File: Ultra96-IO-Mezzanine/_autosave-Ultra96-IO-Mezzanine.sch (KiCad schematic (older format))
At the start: 45 parts, among them J1 USB_C_Receptacle_USB2.0, J2 Conn_01x08_Female, J3 USB_C_Receptacle_USB2.0, P1 CONN_02X20, P2 CONN_02X30, P3 CONN_02X20, Q1 STL6P3LLH6, SW1 SW_SP3T, U1 TXS0104ERGYR, U2 CP2102N-A01-GQFN24, U3 TXS0108EPW, U4 STUSB4500QTR, U5 TXS0108EPW

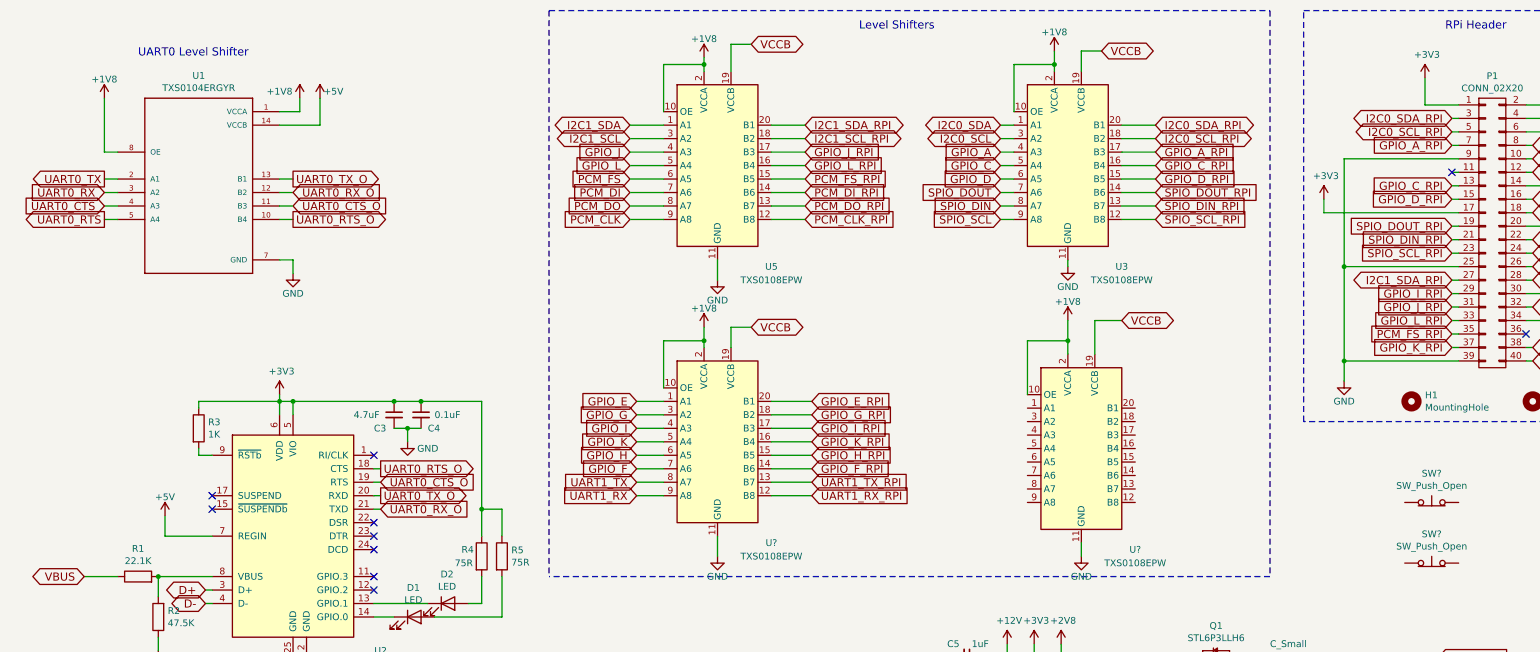
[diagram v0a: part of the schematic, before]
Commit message: Added TXS0108
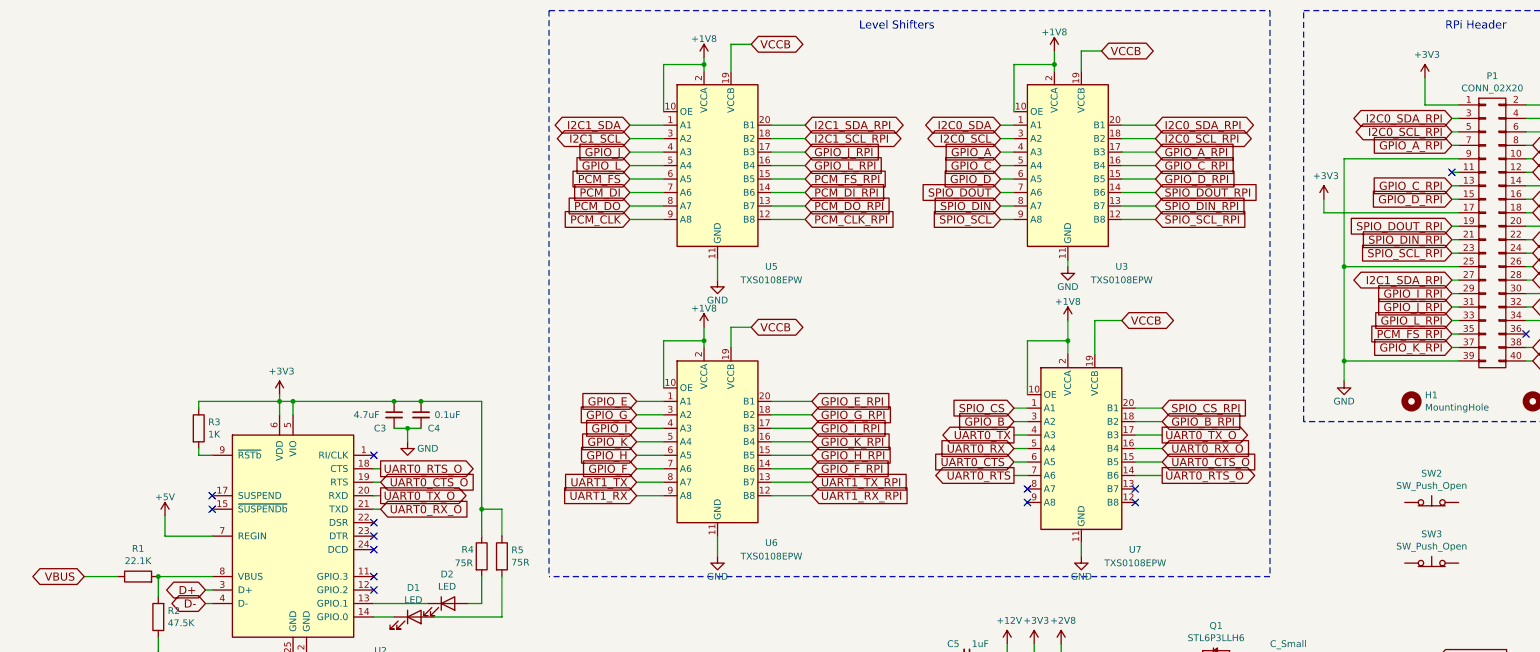
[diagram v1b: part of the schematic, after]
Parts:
- removed U1: TXS0104ERGYR, Package_DFN_QFN:Texas_S-PVQFN-N14_ThermalVias, symbol Ultra96-IO-Mezzanine-rescue:TXS0104ERGYR-LevelShifer
- gave numbers to parts that had none: 4
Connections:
- net GPIO_B: now also U7.3 (A2)
- net GPIO_B_RPI: now also U7.18 (B2)
- net SPIO_CS: now also U7.1 (A1)
- net SPIO_CS_RPI: now also U7.20 (B1)
- net UART0_CTS: now also U7.6 (A5)
- net UART0_CTS_O: now also U7.15 (B5)
- net UART0_RTS: now also U7.7 (A6)
- net UART0_RTS_O: now also U7.14 (B6)
- net UART0_RX: now also U7.5 (A4)
- net UART0_RX_O: now also U7.16 (B4)
- net UART0_TX: now also U7.4 (A3)
- net UART0_TX_O: now also U7.17 (B3)
- no-connect marks 26 -> 30
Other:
- note removed: "UART0 Level Shifter"
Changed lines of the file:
@@
 Wire Notes Line
 	13150 600  13150 4250
-$Comp
-L Ultra96-IO-Mezzanine-rescue:GND-power #PWR07
-U 1 1 5F13E6D4
-P 2900 2550
-F 0 "#PWR07" H 2900 2300 50  0001 C CNN
-F 1 "GND" H 2900 2400 50  0000 C CNN
-F 2 "" H 2900 2550 60  0000 C CNN
-F 3 "" H 2900 2550 60  0000 C CNN
-	1    2900 2550
-	1    0    0    -1
-$EndComp
-Wire Wire Line
-	2900 2450 2900 2550
-Text GLabel 1500 1850 0    60   Output ~ 0
+Text GLabel 8250 3750 0    60   Output ~ 0
 UART0_TX
 Wire Wire Line
-	1500 1850 1600 1850
-Text GLabel 1500 1950 0    60   Input ~ 0
+	8250 3750 8350 3750
+Text GLabel 8250 3850 0    60   Input ~ 0
 UART0_RX
 Wire Wire Line
-	1500 1950 1600 1950
-Text GLabel 1500 2050 0    60   Input ~ 0
+	8250 3850 8350 3850
+Text GLabel 8250 3950 0    60   Input ~ 0
 UART0_CTS
 Wire Wire Line
-	1500 2050 1600 2050
-Text GLabel 1500 2150 0    60   Output ~ 0
+	8250 3950 8350 3950
+Text GLabel 8250 4050 0    60   Output ~ 0
 UART0_RTS
 Wire Wire Line
-	1500 2150 1600 2150
-$Comp
-L Ultra96-IO-Mezzanine-rescue:+5V-power #PWR010
-U 1 1 5F1655F2
-P 3100 1250
-F 0 "#PWR010" H 3100 1100 50  0001 C CNN
-F 1 "+5V" H 3200 1300 50  0000 C CNN
-F 2 "" H 3100 1250 50  0001 C CNN
-F 3 "" H 3100 1250 50  0001 C CNN
-	1    3100 1250
-	1    0    0    -1
-$EndComp
-Text GLabel 2900 1850 2    60   Output ~ 0
+	8250 4050 8350 4050
+Text GLabel 9350 3750 2    60   Output ~ 0
 UART0_TX_O
-Wire Wire Line
-	2900 1850 2800 1850
-Text GLabel 2900 1950 2    60   Input ~ 0
+Text GLabel 9350 3850 2    60   Input ~ 0
 UART0_RX_O
-Wire Wire Line
-	2900 1950 2800 1950
-Text GLabel 2900 2050 2    60   Input ~ 0
+Text GLabel 9350 3950 2    60   Input ~ 0
 UART0_CTS_O
-Wire Wire Line
-	2900 2050 2800 2050
-Text GLabel 2900 2150 2    60   Output ~ 0
+Text GLabel 9350 4050 2    60   Output ~ 0
 UART0_RTS_O
-Wire Wire Line
-	2900 2150 2800 2150
-$Comp
-L Ultra96-IO-Mezzanine-rescue:TXS0104ERGYR-LevelShifer U1
-U 1 1 5F19EA6D
-P 2200 1950
-F 0 "U1" H 2200 2817 50  0000 C CNN
-F 1 "TXS0104ERGYR" H 2200 2726 50  0000 C CNN
-F 2 "Package_DFN_QFN:Texas_S-PVQFN-N14_ThermalVias" H 2200 1950 50  0001 L BNN
-F 3 "TEXAS INSTRUMENTS" H 2200 1950 50  0001 L BNN
-F 4 "IPC 7351B" H 2200 1950 50  0001 L BNN "Field4"
-F 5 "H" H 2200 1950 50  0001 L BNN "Field5"
-	1    2200 1950
-	1    0    0    -1
-$EndComp
-Wire Wire Line
-	2950 1250 2950 1350
-$Comp
-L Ultra96-IO-Mezzanine-rescue:+1V8-power #PWR09
-U 1 1 5F143AFB
-P 2950 1250
-F 0 "#PWR09" H 2950 1100 50  0001 C CNN
-F 1 "+1V8" H 2800 1300 50  0000 C CNN
-F 2 "" H 2950 1250 60  0000 C CNN
-F 3 "" H 2950 1250 60  0000 C CNN
-	1    2950 1250
-	1    0    0    -1
-$EndComp
-Wire Wire Line
-	2800 1350 2950 1350
-Wire Wire Line
-	2800 1450 3100 1450
-Wire Wire Line
-	3100 1250 3100 1450
-Wire Wire Line
-	2900 2450 2800 2450
-$Comp
-L Ultra96-IO-Mezzanine-rescue:+1V8-power #PWR03
-U 1 1 5F1F21A8
-P 1500 1250
-F 0 "#PWR03" H 1500 1100 50  0001 C CNN
-F 1 "+1V8" H 1500 1390 50  0000 C CNN
-F 2 "" H 1500 1250 60  0000 C CNN
-F 3 "" H 1500 1250 60  0000 C CNN
-	1    1500 1250
-	1    0    0    -1
-$EndComp
-Wire Wire Line
-	1500 1250 1500 1650
-Wire Wire Line
-	1500 1650 1600 1650
-Text Notes 1750 950  0    60   ~ 0
-UART0 Level Shifter
 $Comp
 L 96boards:CONN_02X20 P1
@@
 	4800 600  4800 4800
 $Comp
-L Ultra96-IO-Mezzanine-rescue:TXS0108EPW-Logic_LevelTranslator U?
+L Ultra96-IO-Mezzanine-rescue:TXS0108EPW-Logic_LevelTranslator U6
 U 1 1 6087561F
 P 6050 3800
-F 0 "U?" H 6450 3050 50  0000 C CNN
+F 0 "U6" H 6450 3050 50  0000 C CNN
 F 1 "TXS0108EPW" H 6450 2950 50  0000 C CNN
 F 2 "LevelShifter:QFN50P450X350X100-21N" H 6050 3050 50  0001 C CNN
@@
 	6150 2950 6150 3100
 $Comp
-L Ultra96-IO-Mezzanine-rescue:+1V8-power #PWR?
+L Ultra96-IO-Mezzanine-rescue:+1V8-power #PWR0121
 U 1 1 60968362
 P 5950 2950
-F 0 "#PWR?" H 5950 2800 50  0001 C CNN
+F 0 "#PWR0121" H 5950 2800 50  0001 C CNN
 F 1 "+1V8" H 5950 3090 50  0000 C CNN
 F 2 "" H 5950 2950 60  0000 C CNN
@@
 	5950 3050 5950 3100
 $Comp
-L Ultra96-IO-Mezzanine-rescue:GND-power #PWR?
+L Ultra96-IO-Mezzanine-rescue:GND-power #PWR0122
 U 1 1 609E325F
 P 6050 4650
-F 0 "#PWR?" H 6050 4400 50  0001 C CNN
+F 0 "#PWR0122" H 6050 4400 50  0001 C CNN
 F 1 "GND" H 6050 4500 50  0000 C CNN
 F 2 "" H 6050 4650 60  0000 C CNN
@@
 GPIO_F
 $Comp
-L Switch:SW_Push_Open SW?
+L Switch:SW_Push_Open SW2
 U 1 1 60B20626
 P 11350 4250
-F 0 "SW?" H 11350 4465 50  0000 C CNN
+F 0 "SW2" H 11350 4465 50  0000 C CNN
 F 1 "SW_Push_Open" H 11350 4374 50  0000 C CNN
 F 2 "" H 11350 4450 50  0001 C CNN
@@
 $EndComp
 $Comp
-L Switch:SW_Push_Open SW?
+L Switch:SW_Push_Open SW3
 U 1 1 60B20916
 P 11350 4700
-F 0 "SW?" H 11350 4915 50  0000 C CNN
+F 0 "SW3" H 11350 4915 50  0000 C CNN
 F 1 "SW_Push_Open" H 11350 4824 50  0000 C CNN
 F 2 "" H 11350 4900 50  0001 C CNN
@@
 $EndComp
 $Comp
-L Ultra96-IO-Mezzanine-rescue:TXS0108EPW-Logic_LevelTranslator U?
+L Ultra96-IO-Mezzanine-rescue:TXS0108EPW-Logic_LevelTranslator U7
 U 1 1 60B5F573
 P 8750 3850
-F 0 "U?" H 9150 3100 50  0000 C CNN
+F 0 "U7" H 9150 3100 50  0000 C CNN
 F 1 "TXS0108EPW" H 9150 3000 50  0000 C CNN
 F 2 "LevelShifter:QFN50P450X350X100-21N" H 8750 3100 50  0001 C CNN
@@
 $EndComp
 $Comp
-L Ultra96-IO-Mezzanine-rescue:GND-power #PWR?
+L Ultra96-IO-Mezzanine-rescue:GND-power #PWR0123
 U 1 1 60B604BC
 P 8750 4650
-F 0 "#PWR?" H 8750 4400 50  0001 C CNN
+F 0 "#PWR0123" H 8750 4400 50  0001 C CNN
 F 1 "GND" H 8750 4500 50  0000 C CNN
 F 2 "" H 8750 4650 60  0000 C CNN
@@
 	8850 2900 8850 3150
 $Comp
-L Ultra96-IO-Mezzanine-rescue:+1V8-power #PWR?
+L Ultra96-IO-Mezzanine-rescue:+1V8-power #PWR0124
 U 1 1 60BDA8DF
 P 8650 2900
-F 0 "#PWR?" H 8650 2750 50  0001 C CNN
+F 0 "#PWR0124" H 8650 2750 50  0001 C CNN
 F 1 "+1V8" H 8650 3040 50  0000 C CNN
 F 2 "" H 8650 2900 60  0000 C CNN
@@
 Wire Wire Line
 	5450 4200 5650 4200
+Text GLabel 9350 3550 2    60   Input ~ 0
+SPIO_CS_RPI
+Text GLabel 9350 3650 2    60   Input ~ 0
+GPIO_B_RPI
+Wire Wire Line
+	9150 3750 9350 3750
+Wire Wire Line
+	9150 3850 9350 3850
+Wire Wire Line
+	9150 3950 9350 3950
+Wire Wire Line
+	9150 4050 9350 4050
+Wire Wire Line
+	9350 3650 9150 3650
+Wire Wire Line
+	9350 3550 9150 3550
+Text GLabel 8250 3650 0    60   Input ~ 0
+GPIO_B
+Text GLabel 8250 3550 0    60   Input ~ 0
+SPIO_CS
+Wire Wire Line
+	8350 3550 8250 3550
+Wire Wire Line
+	8250 3650 8350 3650
+NoConn ~ 9150 4150
+NoConn ~ 9150 4250
+NoConn ~ 8350 4150
+NoConn ~ 8350 4250
 $EndSCHEMATC
